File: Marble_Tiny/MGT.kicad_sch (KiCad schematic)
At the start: 1 part, among them U1 XC7A35T-CSG325

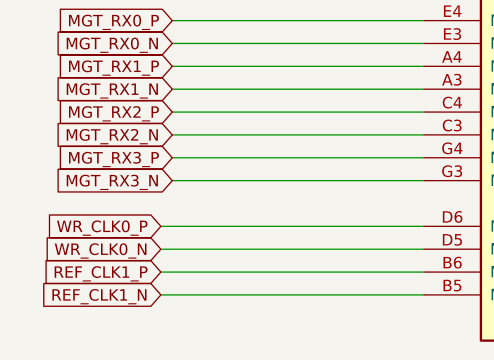
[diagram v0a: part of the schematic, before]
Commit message: components placement done, fixed issue with PCB
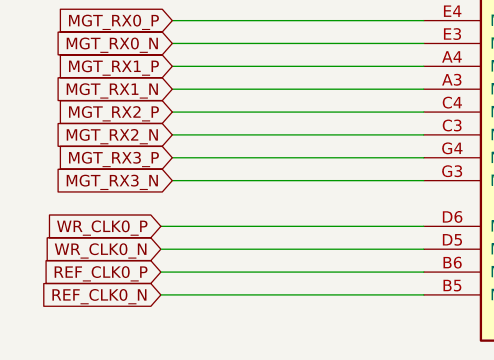
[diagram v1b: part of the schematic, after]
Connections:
- net REF_CLK1_N renamed REF_CLK0_N
- net REF_CLK1_P renamed REF_CLK0_P
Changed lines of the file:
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@@
 (kicad_sch
-	(version 20241209)
+	(version 20250114)
 	(generator "eeschema")
 	(generator_version "9.0")
@@
 		)
 	)
-	(global_label "REF_CLK1_N"
+	(global_label "MGT_RX3_N"
+		(shape input)
+		(at 93.98 92.71 180)
+		(fields_autoplaced yes)
+		(effects
+			(font
+				(size 1.27 1.27)
+			)
+			(justify right)
+		)
+		(property "Intersheetrefs" "${INTERSHEET_REFS}"
+			(at 80.3511 92.71 0)
+			(effects
+				(font
+					(size 1.27 1.27)
+				)
+				(justify right)
+				(hide yes)
+			)
+		)
+	)
+	(global_label "REF_CLK0_N"
 		(shape input)
 		(at 92.71 105.41 180)
@@
 		)
 	)
-	(global_label "REF_CLK1_P"
+	(global_label "MGT_RX0_N"
+		(shape input)
+		(at 93.98 77.47 180)
+		(fields_autoplaced yes)
+		(effects
+			(font
+				(size 1.27 1.27)
+			)
+			(justify right)
+		)
+		(property "Intersheetrefs" "${INTERSHEET_REFS}"
+			(at 80.3511 77.47 0)
+			(effects
+				(font
+					(size 1.27 1.27)
+				)
+				(justify right)
+				(hide yes)
+			)
+		)
+	)
+	(global_label "MGT_TX2_P"
+		(shape output)
+		(at 93.98 62.23 180)
+		(fields_autoplaced yes)
+		(effects
+			(font
+				(size 1.27 1.27)
+			)
+			(justify right)
+		)
+		(property "Intersheetrefs" "${INTERSHEET_REFS}"
+			(at 80.714 62.23 0)
+			(effects
+				(font
+					(size 1.27 1.27)
+				)
+				(justify right)
+				(hide yes)
+			)
+		)
+	)
+	(global_label "MGT_TX1_N"
+		(shape output)
+		(at 93.98 59.69 180)
+		(fields_autoplaced yes)
+		(effects
+			(font
+				(size 1.27 1.27)
+			)
+			(justify right)
+		)
+		(property "Intersheetrefs" "${INTERSHEET_REFS}"
+			(at 80.6535 59.69 0)
+			(effects
+				(font
+					(size 1.27 1.27)
+				)
+				(justify right)
+				(hide yes)
+			)
+		)
+	)
+	(global_label "MGT_TX0_N"
+		(shape output)
+		(at 93.98 54.61 180)
+		(fields_autoplaced yes)
+		(effects
+			(font
+				(size 1.27 1.27)
+			)
+			(justify right)
+		)
+		(property "Intersheetrefs" "${INTERSHEET_REFS}"
+			(at 80.6535 54.61 0)
+			(effects
+				(font
+					(size 1.27 1.27)
+				)
+				(justify right)
+				(hide yes)
+			)
+		)
+	)
+	(global_label "WR_CLK0_N"
+		(shape input)
+		(at 92.71 100.33 180)
+		(fields_autoplaced yes)
+		(effects
+			(font
+				(size 1.27 1.27)
+				(thickness 0.1588)
+			)
+			(justify right)
+		)
+		(property "Intersheetrefs" "${INTERSHEET_REFS}"
+			(at 78.4841 100.33 0)
+			(effects
+				(font
+					(size 1.27 1.27)
+				)
+				(justify right)
+				(hide yes)
+			)
+		)
+	)
+	(global_label "WR_CLK0_P"
+		(shape input)
+		(at 92.71 97.79 180)
+		(fields_autoplaced yes)
+		(effects
+			(font
+				(size 1.27 1.27)
+				(thickness 0.1588)
+			)
+			(justify right)
+		)
+		(property "Intersheetrefs" "${INTERSHEET_REFS}"
+			(at 78.5446 97.79 0)
+			(effects
+				(font
+					(size 1.27 1.27)
+				)
+				(justify right)
+				(hide yes)
+			)
+		)
+	)
+	(global_label "REF_CLK0_P"
 		(shape input)
 		(at 92.71 102.87 180)
@@
 			(effects
 				(font
-					(size 1.27 1.27)
-				)
-				(justify right)
-				(hide yes)
-			)
-		)
-	)
-	(global_label "MGT_RX3_N"
-		(shape input)
-		(at 93.98 92.71 180)
-		(fields_autoplaced yes)
-		(effects
-			(font
-				(size 1.27 1.27)
-			)
-			(justify right)
-		)
-		(property "Intersheetrefs" "${INTERSHEET_REFS}"
-			(at 80.3511 92.71 0)
-			(effects
-				(font
-					(size 1.27 1.27)
-				)
-				(justify right)
-				(hide yes)
-			)
-		)
-	)
-	(global_label "MGT_RX0_N"
-		(shape input)
-		(at 93.98 77.47 180)
-		(fields_autoplaced yes)
-		(effects
-			(font
-				(size 1.27 1.27)
-			)
-			(justify right)
-		)
-		(property "Intersheetrefs" "${INTERSHEET_REFS}"
-			(at 80.3511 77.47 0)
-			(effects
-				(font
-					(size 1.27 1.27)
-				)
-				(justify right)
-				(hide yes)
-			)
-		)
-	)
-	(global_label "MGT_TX2_P"
-		(shape output)
-		(at 93.98 62.23 180)
-		(fields_autoplaced yes)
-		(effects
-			(font
-				(size 1.27 1.27)
-			)
-			(justify right)
-		)
-		(property "Intersheetrefs" "${INTERSHEET_REFS}"
-			(at 80.714 62.23 0)
-			(effects
-				(font
-					(size 1.27 1.27)
-				)
-				(justify right)
-				(hide yes)
-			)
-		)
-	)
-	(global_label "MGT_TX1_N"
-		(shape output)
-		(at 93.98 59.69 180)
-		(fields_autoplaced yes)
-		(effects
-			(font
-				(size 1.27 1.27)
-			)
-			(justify right)
-		)
-		(property "Intersheetrefs" "${INTERSHEET_REFS}"
-			(at 80.6535 59.69 0)
-			(effects
-				(font
-					(size 1.27 1.27)
-				)
-				(justify right)
-				(hide yes)
-			)
-		)
-	)
-	(global_label "MGT_TX0_N"
-		(shape output)
-		(at 93.98 54.61 180)
-		(fields_autoplaced yes)
-		(effects
-			(font
-				(size 1.27 1.27)
-			)
-			(justify right)
-		)
-		(property "Intersheetrefs" "${INTERSHEET_REFS}"
-			(at 80.6535 54.61 0)
-			(effects
-				(font
-					(size 1.27 1.27)
-				)
-				(justify right)
-				(hide yes)
-			)
-		)
-	)
-	(global_label "WR_CLK0_N"
-		(shape input)
-		(at 92.71 100.33 180)
-		(fields_autoplaced yes)
-		(effects
-			(font
-				(size 1.27 1.27)
-				(thickness 0.1588)
-			)
-			(justify right)
-		)
-		(property "Intersheetrefs" "${INTERSHEET_REFS}"
-			(at 78.4841 100.33 0)
-			(effects
-				(font
-					(size 1.27 1.27)
-				)
-				(justify right)
-				(hide yes)
-			)
-		)
-	)
-	(global_label "WR_CLK0_P"
-		(shape input)
-		(at 92.71 97.79 180)
-		(fields_autoplaced yes)
-		(effects
-			(font
-				(size 1.27 1.27)
-				(thickness 0.1588)
-			)
-			(justify right)
-		)
-		(property "Intersheetrefs" "${INTERSHEET_REFS}"
-			(at 78.5446 97.79 0)
-			(effects
-				(font

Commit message: fixed issue with PMODs; added board name and revision; fixed polygons issue
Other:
- company: (none) -> ${name}
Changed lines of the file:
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@@
 	(generator_version "9.0")
 	(paper "A4")
+	(title_block
+		(date "2025-04-18")
+		(rev "${rev}")
+		(company "${name}")
+		(comment 1 "${author}")
+	)
 	(wire
 		(pts
